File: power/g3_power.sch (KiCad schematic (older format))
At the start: 31 parts, among them J101 Conn_Solar_Panel_01x02_Female, J102 Conn_Battery_01x02_Female, U101 RT9471GQW, U102 TPS61202DRC, U103 LM358

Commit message: fixes to power and compute
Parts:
- removed D102: LED_Red, symbol Device:LED_Small
- removed R102: TBD, symbol Device:R_Small_US
- removed R103: 250k, symbol Device:R_Small_US
- added D1: LED_Green, LED_SMD:LED_0603_1608Metric_Pad1.05x0.95mm_HandSolder, symbol Device:LED_Small
- added R1: 2.2k, Resistor_SMD:R_0805_2012Metric_Pad1.20x1.40mm_HandSolder, symbol Device:R_Small_US
- C101, C102, C103, C104, C105, C106, C107: footprint (none) -> Capacitor_SMD:C_0603_1608Metric_Pad1.08x0.95mm_HandSolder
- C108: value TBD -> 0.1uF; footprint (none) -> Capacitor_SMD:C_0603_1608Metric_Pad1.08x0.95mm_HandSolder
- D101: footprint (none) -> LED_SMD:LED_0603_1608Metric_Pad1.05x0.95mm_HandSolder
- L101: footprint (none) -> Inductor_SMD:L_0603_1608Metric_Pad1.05x0.95mm_HandSolder
- L102: value TBD -> 1uH; footprint (none) -> Inductor_SMD:L_0603_1608Metric_Pad1.05x0.95mm_HandSolder
- R101: value TBD -> 2.2k; footprint (none) -> Resistor_SMD:R_0805_2012Metric_Pad1.20x1.40mm_HandSolder
- R104, R105, R106, R107, R108, R109, R110, R111, R112: footprint (none) -> Resistor_SMD:R_0805_2012Metric_Pad1.20x1.40mm_HandSolder
- gave numbers to parts that had none: 1
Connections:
- wire segments 148 -> 150
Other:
- note removed: "Note: \nData sheet unclear, might \nbe internall implemented"

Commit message: added footprints
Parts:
- J1: footprint (none) -> Perch:532611071_Molex
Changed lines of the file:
@@
 F 0 "J1" H 2000 7275 50  0000 L CNN
 F 1 "Conn_Power_Compute_01x10_Female" H 2000 7350 50  0000 L CNN
-F 2 "" H 3125 6800 50  0001 C CNN
+F 2 "Perch:532611071_Molex" H 3125 6800 50  0001 C CNN
 F 3 "~" H 3125 6800 50  0001 C CNN
 	1    3125 6800

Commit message: Making changes suggested
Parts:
- removed J1: Conn_Power_Compute_01x10_Female, Perch:532611071_Molex, symbol Connector:Conn_01x10_Female
- removed R106: 10k, Resistor_SMD:R_0805_2012Metric_Pad1.20x1.40mm_HandSolder, symbol Device:R_Small_US
- added J?: 53261-1071, 532611071, symbol 53261-1071:53261-1071
- R112: value 1ok -> 10k
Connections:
- net labels added: +5V, CC_REGN, CC_SYS, V_BATT, V_REGN, V_SOL
- net labels removed: 5V, 5v, VCC_REGN, VCC_SYS
- wire segments 150 -> 147
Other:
- note added: "Note: REGN LDO is 5V when \nexternal power applied, \notherwise off to save power"
- note added: "Question: \nWhat do these do?"
- note added: "TODO: Add ADC\nconnections"
- note added: "TODO: Add adc module to this \nschematic, Ideal using a I2C module"
- note removed: "IMPORTANT: \nOnly load one\npull resistor!"
- moved on the sheet: D1, D101, J102, R1, R101, R104

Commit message: Major changes to Power sch
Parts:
- added JP1, JP2, JP3: SolderJumper_2_Bridged, symbol Jumper:SolderJumper_2_Bridged
- added SW1: SW_Push, symbol Switch:SW_Push
- D101: value LED_Green -> LED_Red
- J1: renamed from J?; footprint 532611071 -> (none)
- J101, J102: footprint (none) -> Perch:532610271_Molex
- L102: value 1uH -> 2.2uH
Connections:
- net labels removed: CC_REGN, CC_RGEN, CC_VBUS, VAUX, VBAT, VR_EN, VSOL
- wire segments 147 -> 177
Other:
- note added: "Note: Set to High for \ncurrent limit to using 0.5A \n(Software can set this for later)"
- note removed: "Power Flags"
- note removed: "Question: \nWhat do these do?"
- moved on the sheet: C101, C102, C103, D101, J1, J101, J102, L102, R101, R104, R105, R107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

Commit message: added new VR
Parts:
- removed C108: 0.1uF, Capacitor_SMD:C_0603_1608Metric_Pad1.08x0.95mm_HandSolder, symbol Device:C
- removed U102: TPS61202DRC, Package_SON:Texas_S-PVSON-N10_ThermalVias, symbol Regulator_Switching:TPS61202DRC
- added U1: TPS613222ADBV, Package_TO_SOT_SMD:SOT-23-5, symbol Regulator_Switching:TPS613222ADBV
- R107: value 5.23k -> 10k
- R108: value 30.1k -> 10k
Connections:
- net labels removed: VR_PS
- wire segments 177 -> 147
- no-connect marks 0 -> 3
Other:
- note added: "Note: \nUsed 2 x 10k Ohm if \ntemperature sensing \nNOT used"
- note added: "Note: \nUsed 5.23k x 30.1k Ohm if\ntemperature sensing \nIS used"
- note removed: "Note: \nPlace near SYS pin\n"
- note removed: "Note: \nUsed 2 x 10k Ohm if \ntemperature sensing \nnot used"
- note removed: "TODO: Add ADC\nconnections"
- moved on the sheet: L102

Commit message: adding ADC and old VR
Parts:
- removed U1: TPS613222ADBV, Package_TO_SOT_SMD:SOT-23-5, symbol Regulator_Switching:TPS613222ADBV
- added C? (x2): 0.1uF, Capacitor_SMD:C_0603_1608Metric_Pad1.08x0.95mm_HandSolder, symbol Device:C_Small
- added C?: 10uF, Capacitor_SMD:C_0603_1608Metric_Pad1.08x0.95mm_HandSolder, symbol Device:C_Small
- added U?: MCP3422, symbol Analog_ADC:MCP3422
- added U?: TPS61202DRC, Package_SON:Texas_S-PVSON-N10_ThermalVias, symbol Regulator_Switching:TPS61202DRC
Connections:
- net labels added: VR_PS
- wire segments 147 -> 193
- no-connect marks 3 -> 2
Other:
- note added: "ADC"
- note added: "NOTE:\nI don't think this is \nthe correct config. \nMight need to be \nlooked at further."
- note added: "Note: \nPlace near Vdd pin"
- note added: "Note: \nPlace near switch \nVR input"
- moved on the sheet: L102

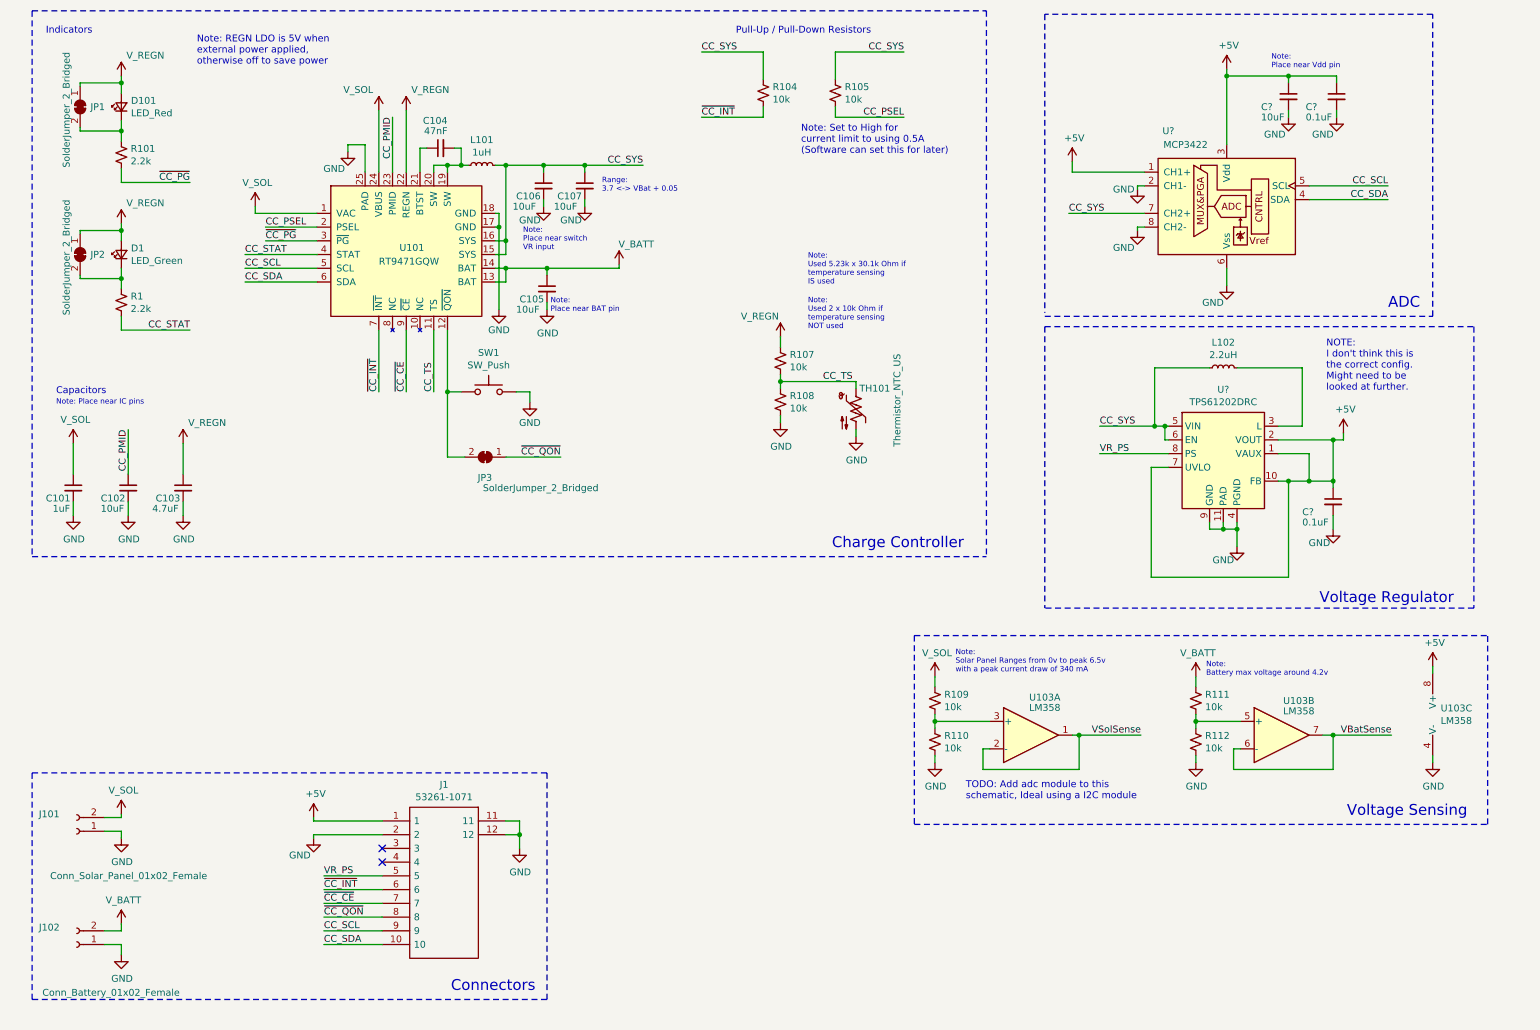
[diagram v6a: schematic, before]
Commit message: changes to power symbols and bypass caps
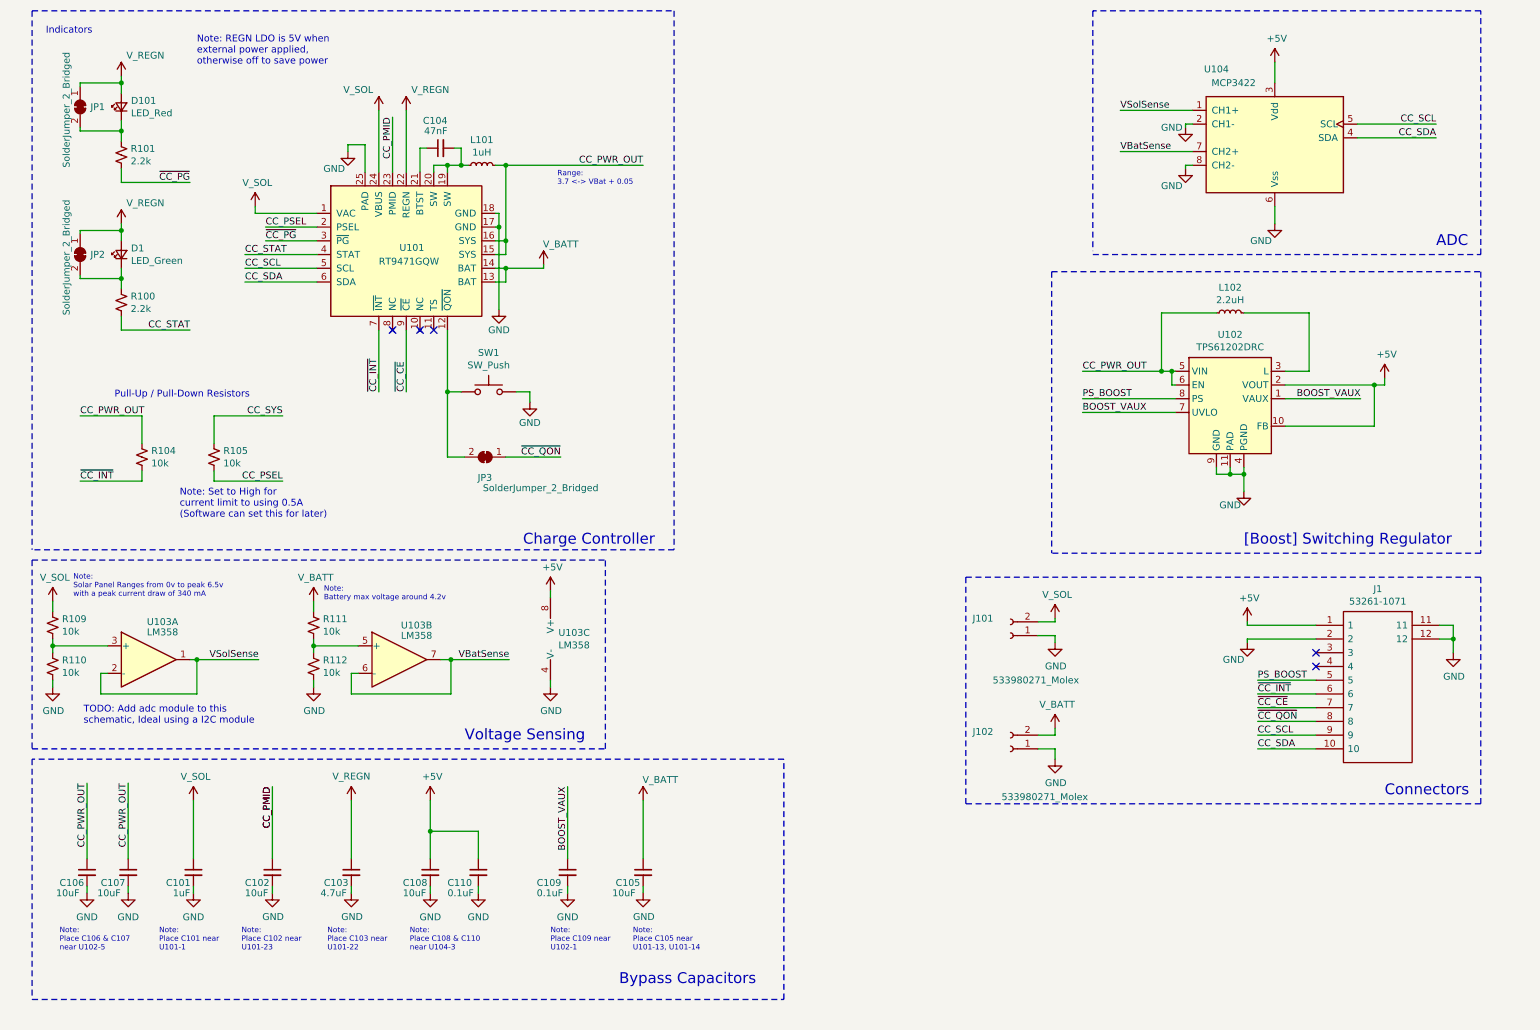
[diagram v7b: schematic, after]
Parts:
- removed R107, R108: 10k, Resistor_SMD:R_0805_2012Metric_Pad1.20x1.40mm_HandSolder, symbol Device:R_Small_US
- removed TH101: Thermistor_NTC_US, symbol Device:Thermistor_NTC_US
- removed U?: MCP3422, symbol Analog_ADC:MCP3422
- added U104: MCP3422, symbol MCP3422:MCP3422
- J101: value Conn_Solar_Panel_01x02_Female -> 533980271_Molex
- J102: value Conn_Battery_01x02_Female -> 533980271_Molex
- gave numbers to parts that had none: 4
- renumbered R1 to R100
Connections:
- net +5V: now also U104.3 (Vdd); no longer C109.1, U102.1 (VAUX), U102.7 (UVLO)
- net CC_SCL: now also U104.5 (SCL)
- net CC_SDA: now also U104.4 (SDA)
- net CC_SYS: no longer C106.1, C107.1, L101.2, L102.1, R104.1, U101.15 (SYS), U101.16 (SYS), U102.5 (VIN), U102.6 (EN)
- net GND: now also U104.2 (CH1-), U104.6 (Vss), U104.8 (CH2-)
- net VBatSense: now also U104.7 (CH2+)
- net VSolSense: now also U104.1 (CH1+)
- net CC_TS: no longer names the net of U101.11 (TS)
- net VR_PS renamed PS_BOOST
- new net BOOST_VAUX: C109.1, U102.1 (VAUX), U102.7 (UVLO)
- new net CC_PWR_OUT: C106.1, C107.1, L101.2, L102.1, R104.1, U101.15 (SYS), U101.16 (SYS), U102.5 (VIN), U102.6 (EN)
- no-connect marks 2 -> 5
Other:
- note added: "Bypass Capacitors"
- note added: "Note: \nPlace C101 near \nU101-1"
- note added: "Note: \nPlace C102 near \nU101-23"
- note added: "Note: \nPlace C103 near \nU101-22"
- note added: "Note: \nPlace C105 near \nU101-13, U101-14\n"
- note added: "Note: \nPlace C106 & C107 \nnear U102-5"
- note added: "Note: \nPlace C108 & C110 \nnear U104-3"
- note added: "Note: \nPlace C109 near \nU102-1"
- note added: "[Boost] Switching Regulator"
- note removed: "Capacitors"
- note removed: "NOTE:\nI don't think this is \nthe correct config. \nMight need to be \nlooked at further."
- note removed: "Note: Place near IC pins"
- note removed: "Note: \nPlace near BAT pin\n"
- note removed: "Note: \nPlace near Vdd pin"
- note removed: "Note: \nPlace near switch \nVR input"
- note removed: "Note: \nUsed 2 x 10k Ohm if \ntemperature sensing \nNOT used"
- note removed: "Note: \nUsed 5.23k x 30.1k Ohm if\ntemperature sensing \nIS used"
- note removed: "Voltage Regulator"
- moved on the sheet: C101, C102, C103, C105, C106, C107, C108, C109, C110, J1, J101, J102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

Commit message: made changes and layout
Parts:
- removed J1: 53261-1071, symbol 53261-1071:53261-1071
- added J103: 53398-0871, Perch:53398-0871_Molex, symbol 533980871_Molex:53398-0871
- added R102, R103, R106: 10k, Resistor_SMD:R_0402_1005Metric_Pad0.72x0.64mm_HandSolder, symbol Device:R_Small_US
- C104: footprint Capacitor_SMD:C_0603_1608Metric_Pad1.08x0.95mm_HandSolder -> Capacitor_SMD:C_0805_2012Metric_Pad1.18x1.45mm_HandSolder
- D101: footprint LED_SMD:LED_0603_1608Metric_Pad1.05x0.95mm_HandSolder -> LED_SMD:LED_0402_1005Metric_Pad0.77x0.64mm_HandSolder
- D102: renamed from D1; footprint LED_SMD:LED_0603_1608Metric_Pad1.05x0.95mm_HandSolder -> LED_SMD:LED_0402_1005Metric_Pad0.77x0.64mm_HandSolder
- JP1, JP2, JP3: footprint (none) -> Jumper:SolderJumper-2_P1.3mm_Bridged_RoundedPad1.0x1.5mm
- L101: footprint Inductor_SMD:L_0603_1608Metric_Pad1.05x0.95mm_HandSolder -> Inductor_SMD:L_1008_2520Metric_Pad1.43x2.20mm_HandSolder
- L102: footprint Inductor_SMD:L_0603_1608Metric_Pad1.05x0.95mm_HandSolder -> Inductor_SMD:L_0805_2012Metric_Pad1.15x1.40mm_HandSolder
- R100, R101, R104, R105, R109, R110, R111, R112: footprint Resistor_SMD:R_0805_2012Metric_Pad1.20x1.40mm_HandSolder -> Resistor_SMD:R_0402_1005Metric_Pad0.72x0.64mm_HandSolder
- SW1: footprint (none) -> digikey-footprints:Switch_Tactile_SMD_6x6mm_PTS645
- U101: footprint Perch:RT9471GQW -> Package_DFN_QFN:WQFN-24-1EP_4x4mm_P0.5mm_EP2.6x2.6mm_ThermalVias
- U103, U104: footprint (none) -> Package_SO:SOIC-8_3.9x4.9mm_P1.27mm
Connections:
- net CC_SYS is gone; now on net CC_PWR_OUT: R105.1
- net +5V: now also J103.1
- net CC_SCL: now also J103.7
- net CC_SDA: now also J103.8
- net GND: now also J103.2, R103.2, R106.2
- net V_REGN: now also R102.1
- net ~CC_CE: now also J103.5
- net ~CC_INT: now also J103.4
- net ~CC_QON: now also J103.6
- net CC_TS: now reaches U101.11 (TS)
- net CC_TS: now also R102.2, R103.1
- net CC_PMID renamed CC_PIMD
- net PS_BOOST renamed BOOST_PS
- net BOOST_PS: now also J103.3, R106.1
- no-connect marks 5 -> 2
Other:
- note added: "Note: Config when\nTS pin is not used"
- moved on the sheet: C104, JP3, L101, R104, R105, SW1, U101
